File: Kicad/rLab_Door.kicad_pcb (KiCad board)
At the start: 4 copper layers, 99.1 x 99.1 mm, 95 parts, among them J1 ACT_1, J10 I2C DISPLAY, J11 PROG, J12 PI, J14 TEST POINTS, J2 V_IN, J3 ACT_2, J4 BATTERY, J5 NPX_1, J6 NPX_2, J7 TAMPER, J8 WIEGAND KEYPAD, J9 NFC SERIAL, Q1 2N7002, Q10 MMBT5551L, Q11 2N7002, Q12 2N7002, Q2 2N7002, Q3 AO3401A, Q4 MMBT5551L, Q5 2N7002, Q6 2N7002, Q7 AO3401A, Q8 2N7002, Q9 2N7002, SW1 RESET, SW2 TEST_1, SW3 TEST_2, SW4 BOOT, U1 MP1584, U2 LM317_TO-252, U3 AMS1117-3.3, U4 ESP32-WROOM-32D

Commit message: Rework of power circuits to improve protection
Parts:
- removed the J2 at (110.0, 140.0)
- removed the J4 at (124.0, 140.0)
- removed the R4 at (118.0, 97.0)
- removed REF** (x4): MountingHole_3.2mm_M3_Pad_Via, MountingHole:MountingHole_3.2mm_M3_Pad_Via
- added D3: SS210, Diode_SMD:D_SMA, F.Cu at (122.5, 100.0)
- added J10: BATTERY, TerminalBlock_Phoenix:TerminalBlock_Phoenix_MPT-0,5-2-2.54_1x02_P2.54mm_Horizontal, F.Cu at (124.5, 140.0)
- added J9: V_IN, TerminalBlock_Phoenix:TerminalBlock_Phoenix_MPT-0,5-2-2.54_1x02_P2.54mm_Horizontal, F.Cu at (110.2, 140.5)
- added RV1: 3k, Potentiometer_THT:Potentiometer_Bourns_3296W_Vertical, F.Cu at (105.5, 98.5)
- F1: value 3A -> 2A
- moved D1 7.50 mm to (114.5, 100.0), turned to 180 degrees
- moved R2 6.23 mm to (123.5, 93.0)
- moved R3 6.23 mm to (119.5, 95.0)
- moved U2 6.23 mm to (114.5, 92.0)
- moved D2 2.55 mm to (128.5, 97.5)
- moved F2 0.50 mm to (125.5, 106.8)
- renumbered D3 to D4, D4 to D5, D5 to D6, D6 to D7, D7 to D8, D8 to D9, J14 to J13, J3 to J2, J5 to J3, J6 to J4, J8 to J5, J9 to J6, J10 to J7, J7 to J8, R9 to R10, R10 to R11, R11 to R12, R14 to R13, R16 to R14, R18 to R15, R15 to R16, R19 to R17, R17 to R18, R20 to R19, R21 to R20, R22 to R21, R23 to R22, R24 to R23, R25 to R24, R26 to R25, R27 to R26, R28 to R27, R29 to R28, R30 to R29, R31 to R30, R32 to R31, R33 to R32, R34 to R33, R35 to R34, R36 to R35, R37 to R36, R38 to R37, R39 to R38, R40 to R39, R5 to R4, R41 to R40, R6 to R5, R8 to R6, R12 to R7, R7 to R8, R13 to R9, SW4 to SW2, SW2 to SW3, SW3 to SW4
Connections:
- D1 pad 2: GND -> Net-(D1-Pad2)
- D2 pad 2: GND -> Net-(D3-Pad1)
- F1 pad 1: V_IN -> Net-(D1-Pad2)
- F2 pad 1: +BATT -> Net-(D3-Pad1)
- R2 pad 2: +BATT -> Net-(D3-Pad1)
- R3 pad 1: +BATT -> Net-(D3-Pad1)
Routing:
- net +BATT: track 108.7 -> 62.8 mm, vias 3 -> 4
- net Net-(D3-Pad1): track 0.00 -> 24.1 mm
- net V_IN: track 103.5 -> 91.6 mm
- net Net-(D1-Pad2): track 0.00 -> 7.37 mm
- net Net-(RV1-Pad1): track 10.5 -> 17.4 mm
- net Net-(U2-Pad2): track 14.9 -> 9.02 mm
- net GND: track 105.2 -> 102.3 mm, vias 14 -> 12
- net +5V: track 164.0 -> 164.8 mm
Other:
- board text added: "#1"
- board text added: "#2"
- board text added: "2.5A"
- board text added: "2A"
- board text added: "3A"
- board text added: "Adjust for 5V output"
- board text added: "Before connecting battery Adjust for 13.75V on V_BATT"
- board text added: "HB"
- board text added: "Made for"
- board text added: "NFC Door Controller (V0.1 2022)"
- board text added: "PWD"
- board text added: "RPi"
- board text added: "RX▶"
- board text added: "TX▶"
- board text added: "↘"
- board text removed: "NFC Door V0.1"

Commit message: Improved V_IN and BATTERY traces to handle up to 4A current
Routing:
- net Net-(F1-Pad2): track 0.00 -> 11.6 mm
- net Net-(F2-Pad2): track 0.00 -> 11.2 mm
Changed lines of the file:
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@@
   (segment (start 137.574391 130.341493) (end 137.580631 130.347733) (width 0.25) (layer "F.Cu") (net 7))
   (segment (start 145.202718 128.852099) (end 145.202718 130.355967) (width 0.25) (layer "F.Cu") (net 8))
+  (segment (start 110.23 130.02) (end 111 129.25) (width 2) (layer "F.Cu") (net 9))
+  (segment (start 110.23 140.5) (end 110.23 130.02) (width 2) (layer "F.Cu") (net 9))
+  (segment (start 124.5 130.25) (end 125.5 129.25) (width 2) (layer "F.Cu") (net 10))
+  (segment (start 124.5 140) (end 124.5 130.25) (width 2) (layer "F.Cu") (net 10))
   (segment (start 164 129.25) (end 164 140) (width 1.5) (layer "F.Cu") (net 11))
   (segment (start 146.922911 132.388495) (end 146.922911 131.500537) (width 0.25) (layer "F.Cu") (net 11))

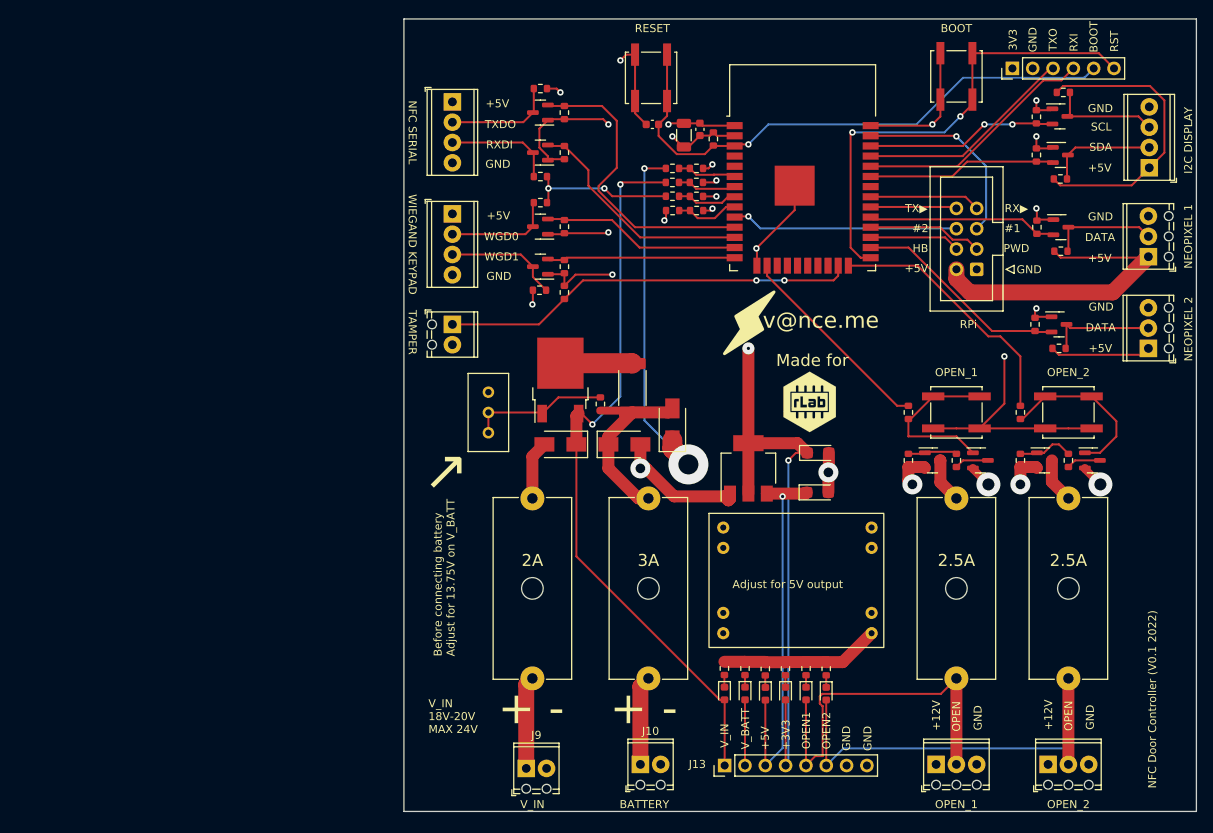
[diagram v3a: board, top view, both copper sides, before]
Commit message: Rounded corners of the board, added M3 mounting holes and recentered components
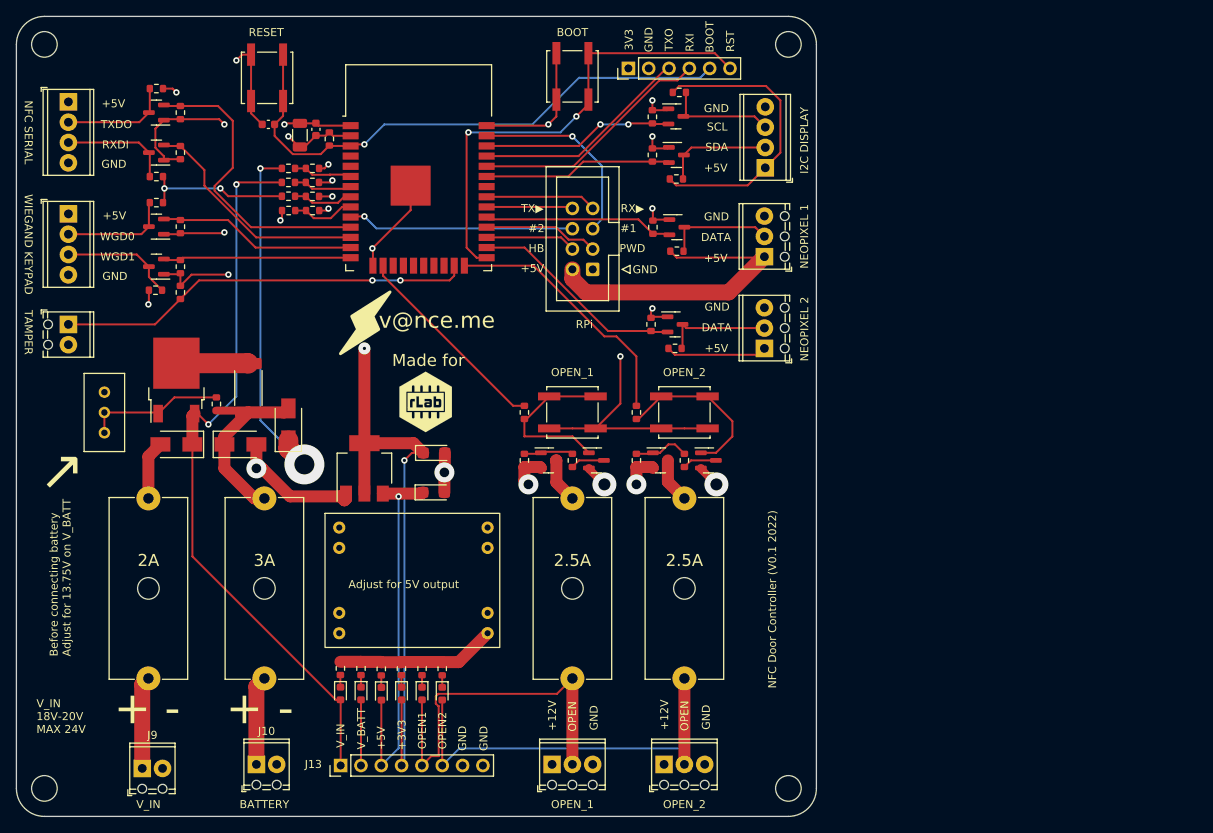
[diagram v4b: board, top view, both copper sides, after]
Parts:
- added REF**: MountingHole_3.2mm_M3_DIN965, MountingHole:MountingHole_3.2mm_M3_DIN965, F.Cu at (143.0, 50.0)
- added REF**: MountingHole_3.2mm_M3_DIN965, MountingHole:MountingHole_3.2mm_M3_DIN965, F.Cu at (50.0, 50.0)
- added REF**: MountingHole_3.2mm_M3_DIN965, MountingHole:MountingHole_3.2mm_M3_DIN965, F.Cu at (50.0, 143.0)
- added REF**: MountingHole_3.2mm_M3_DIN965, MountingHole:MountingHole_3.2mm_M3_DIN965, F.Cu at (143.0, 143.0)
- moved C2 48.0 mm to (98.7, 101.1)
- moved D5 48.0 mm to (89.6, 131.1)
- moved D7 48.0 mm to (99.7, 131.2)
- moved J1 48.0 mm to (113.5, 140.0)
- moved J2 48.0 mm to (127.5, 140.0)
- moved R12 48.0 mm to (99.7, 128.0)
- moved R18 48.0 mm to (94.6, 128.0)
- moved R22 48.0 mm to (125.8, 85.0)
- moved J9 48.0 mm to (62.2, 140.5)
- moved C1 48.0 mm to (98.7, 106.0)
- moved C3 48.0 mm to (81.9, 61.3)
- moved C4 48.0 mm to (83.9, 60.6)
- moved C5 48.0 mm to (78.0, 60.0)
- moved D1 48.0 mm to (66.5, 100.0)
- moved D2 48.0 mm to (80.5, 97.5)
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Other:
- board size 99.1 x 99.1 mm -> 100 x 100 mm
